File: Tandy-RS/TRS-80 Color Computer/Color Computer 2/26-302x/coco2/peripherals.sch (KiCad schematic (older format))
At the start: 44 parts, among them J1 Left Joystick, J2 Right Joystick, J3 RS232, J4 Cassette, J5 Conn_01x16_Female, K1 HB1-DC5V-H62, Q1 2N3055, U1 SC77527P, U2 6821, U3 SC77526, U7 6822

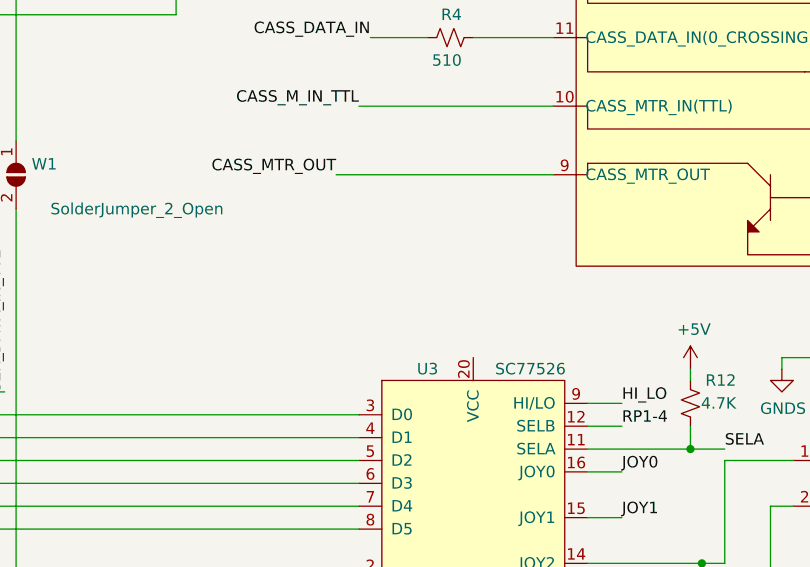
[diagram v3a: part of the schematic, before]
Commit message: connected all of the sheets
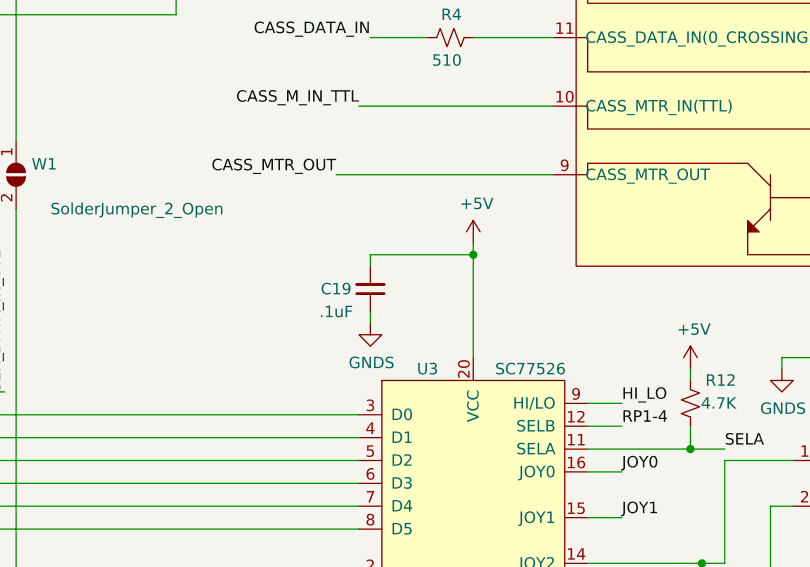
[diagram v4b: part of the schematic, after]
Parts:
- added C19: .1uF, Capacitor_THT:C_Axial_L3.8mm_D2.6mm_P10.00mm_Horizontal, symbol Device:C_Small
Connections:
- net +5V: now also U3.20 (VCC), C19.2
- net GNDS: now also C19.1
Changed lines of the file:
@@
 P 10000 1400
 AR Path="/602A51A8/60A871AE" Ref="#PWR?"  Part="1"
-AR Path="/603CF7B8/60A871AE" Ref="#PWR?"  Part="1"
-F 0 "#PWR?" H 10000 1150 50  0001 C CNN
+AR Path="/603CF7B8/60A871AE" Ref="#PWR0164"  Part="1"
+F 0 "#PWR0164" H 10000 1150 50  0001 C CNN
 F 1 "GNDS" H 10005 1227 50  0000 C CNN
 F 2 "" H 10000 1400 50  0001 C CNN
@@
 P 8850 4250
 AR Path="/602A51A8/60A871C7" Ref="#PWR?"  Part="1"
-AR Path="/603CF7B8/60A871C7" Ref="#PWR?"  Part="1"
-F 0 "#PWR?" H 8850 4000 50  0001 C CNN
+AR Path="/603CF7B8/60A871C7" Ref="#PWR0165"  Part="1"
+F 0 "#PWR0165" H 8850 4000 50  0001 C CNN
 F 1 "GNDS" H 8855 4077 50  0000 C CNN
 F 2 "" H 8850 4250 50  0001 C CNN
@@
 P 9400 2800
 AR Path="/602A51A8/60A871CF" Ref="#PWR?"  Part="1"
-AR Path="/603CF7B8/60A871CF" Ref="#PWR?"  Part="1"
-F 0 "#PWR?" H 9400 2550 50  0001 C CNN
+AR Path="/603CF7B8/60A871CF" Ref="#PWR0166"  Part="1"
+F 0 "#PWR0166" H 9400 2550 50  0001 C CNN
 F 1 "GNDS" H 9405 2627 50  0000 C CNN
 F 2 "" H 9400 2800 50  0001 C CNN
@@
 AR Path="/60273794/60A871FF" Ref="#PWR?"  Part="1"
 AR Path="/602A51A8/60A871FF" Ref="#PWR?"  Part="1"
-AR Path="/603CF7B8/60A871FF" Ref="#PWR?"  Part="1"
-F 0 "#PWR?" H 10400 2250 50  0001 C CNN
+AR Path="/603CF7B8/60A871FF" Ref="#PWR0167"  Part="1"
+F 0 "#PWR0167" H 10400 2250 50  0001 C CNN
 F 1 "+5V" H 10415 2573 50  0000 C CNN
 F 2 "" H 10400 2400 50  0001 C CNN
@@
 P 10250 2100
 AR Path="/602A51A8/60A87208" Ref="#FLG?"  Part="1"
-AR Path="/603CF7B8/60A87208" Ref="#FLG?"  Part="1"
-F 0 "#FLG?" H 10250 2175 50  0001 C CNN
+AR Path="/603CF7B8/60A87208" Ref="#FLG0101"  Part="1"
+F 0 "#FLG0101" H 10250 2175 50  0001 C CNN
 F 1 "PWR_FLAG" H 10250 2273 50  0000 C CNN
 F 2 "" H 10250 2100 50  0001 C CNN
@@
 P 3250 4050
 AR Path="/602A51A8/60BDD9E3" Ref="#PWR?"  Part="1"
-AR Path="/603CF7B8/60BDD9E3" Ref="#PWR?"  Part="1"
-F 0 "#PWR?" H 3250 3800 50  0001 C CNN
+AR Path="/603CF7B8/60BDD9E3" Ref="#PWR0168"  Part="1"
+F 0 "#PWR0168" H 3250 3800 50  0001 C CNN
 F 1 "GNDS" H 3255 3877 50  0000 C CNN
 F 2 "" H 3250 4050 50  0001 C CNN
@@
 AR Path="/60273794/60BE31ED" Ref="#PWR?"  Part="1"
 AR Path="/602A51A8/60BE31ED" Ref="#PWR?"  Part="1"
-AR Path="/603CF7B8/60BE31ED" Ref="#PWR?"  Part="1"
-F 0 "#PWR?" H 2950 650 50  0001 C CNN
+AR Path="/603CF7B8/60BE31ED" Ref="#PWR0169"  Part="1"
+F 0 "#PWR0169" H 2950 650 50  0001 C CNN
 F 1 "+5V" H 2965 973 50  0000 C CNN
 F 2 "" H 2950 800 50  0001 C CNN
@@
 P 4300 1300
 AR Path="/602A51A8/60CCA7E6" Ref="#PWR?"  Part="1"
-AR Path="/603CF7B8/60CCA7E6" Ref="#PWR?"  Part="1"
-F 0 "#PWR?" H 4300 1050 50  0001 C CNN
+AR Path="/603CF7B8/60CCA7E6" Ref="#PWR0170"  Part="1"
+F 0 "#PWR0170" H 4300 1050 50  0001 C CNN
 F 1 "GNDS" H 4150 1250 50  0000 C CNN
 F 2 "" H 4300 1300 50  0001 C CNN
@@
 AR Path="/60273794/60DBF928" Ref="#PWR?"  Part="1"
 AR Path="/602A51A8/60DBF928" Ref="#PWR?"  Part="1"
-AR Path="/603CF7B8/60DBF928" Ref="#PWR?"  Part="1"
-F 0 "#PWR?" H 600 6700 50  0001 C CNN
+AR Path="/603CF7B8/60DBF928" Ref="#PWR0171"  Part="1"
+F 0 "#PWR0171" H 600 6700 50  0001 C CNN
 F 1 "+5V" H 615 7023 50  0000 C CNN
 F 2 "" H 600 6850 50  0001 C CNN
@@
 P 2100 900
 AR Path="/602A51A8/60E75DAA" Ref="#PWR?"  Part="1"
-AR Path="/603CF7B8/60E75DAA" Ref="#PWR?"  Part="1"
-F 0 "#PWR?" H 2100 650 50  0001 C CNN
+AR Path="/603CF7B8/60E75DAA" Ref="#PWR0172"  Part="1"
+F 0 "#PWR0172" H 2100 650 50  0001 C CNN
 F 1 "GNDS" H 2105 727 50  0000 C CNN
 F 2 "" H 2100 900 50  0001 C CNN
@@
 AR Path="/60273794/60E8A73C" Ref="#PWR?"  Part="1"
 AR Path="/602A51A8/60E8A73C" Ref="#PWR?"  Part="1"
-AR Path="/603CF7B8/60E8A73C" Ref="#PWR?"  Part="1"
-F 0 "#PWR?" H 3000 4200 50  0001 C CNN
+AR Path="/603CF7B8/60E8A73C" Ref="#PWR0173"  Part="1"
+F 0 "#PWR0173" H 3000 4200 50  0001 C CNN
 F 1 "+5V" H 3015 4523 50  0000 C CNN
 F 2 "" H 3000 4350 50  0001 C CNN
@@
 P 2150 4450
 AR Path="/602A51A8/60E8A74F" Ref="#PWR?"  Part="1"
-AR Path="/603CF7B8/60E8A74F" Ref="#PWR?"  Part="1"
-F 0 "#PWR?" H 2150 4200 50  0001 C CNN
+AR Path="/603CF7B8/60E8A74F" Ref="#PWR0174"  Part="1"
+F 0 "#PWR0174" H 2150 4200 50  0001 C CNN
 F 1 "GNDS" H 2155 4277 50  0000 C CNN
 F 2 "" H 2150 4450 50  0001 C CNN
@@
 P 3000 7650
 AR Path="/602A51A8/60EC0CD2" Ref="#PWR?"  Part="1"
-AR Path="/603CF7B8/60EC0CD2" Ref="#PWR?"  Part="1"
-F 0 "#PWR?" H 3000 7400 50  0001 C CNN
+AR Path="/603CF7B8/60EC0CD2" Ref="#PWR0175"  Part="1"
+F 0 "#PWR0175" H 3000 7400 50  0001 C CNN
 F 1 "GNDS" H 3005 7477 50  0000 C CNN
 F 2 "" H 3000 7650 50  0001 C CNN
@@
 AR Path="/60273794/60EDF4D8" Ref="#PWR?"  Part="1"
 AR Path="/602A51A8/60EDF4D8" Ref="#PWR?"  Part="1"
-AR Path="/603CF7B8/60EDF4D8" Ref="#PWR?"  Part="1"
-F 0 "#PWR?" H 4400 5900 50  0001 C CNN
+AR Path="/603CF7B8/60EDF4D8" Ref="#PWR0176"  Part="1"
+F 0 "#PWR0176" H 4400 5900 50  0001 C CNN
 F 1 "+5V" H 4415 6223 50  0000 C CNN
 F 2 "" H 4400 6050 50  0001 C CNN
@@
 AR Path="/60273794/60F3326E" Ref="#PWR?"  Part="1"
 AR Path="/602A51A8/60F3326E" Ref="#PWR?"  Part="1"
-AR Path="/603CF7B8/60F3326E" Ref="#PWR?"  Part="1"
-F 0 "#PWR?" H 6950 4650 50  0001 C CNN
+AR Path="/603CF7B8/60F3326E" Ref="#PWR0177"  Part="1"
+F 0 "#PWR0177" H 6950 4650 50  0001 C CNN
 F 1 "+5V" H 6965 4973 50  0000 C CNN
 F 2 "" H 6950 4800 50  0001 C CNN
@@
 P 6000 6900
 AR Path="/602A51A8/611F4F3A" Ref="#PWR?"  Part="1"
-AR Path="/603CF7B8/611F4F3A" Ref="#PWR?"  Part="1"
-F 0 "#PWR?" H 6000 6650 50  0001 C CNN
+AR Path="/603CF7B8/611F4F3A" Ref="#PWR0178"  Part="1"
+F 0 "#PWR0178" H 6000 6650 50  0001 C CNN
 F 1 "GNDS" H 6005 6727 50  0000 C CNN
 F 2 "" H 6000 6900 50  0001 C CNN
@@
 P 7500 5700
 AR Path="/602A51A8/6126A799" Ref="#PWR?"  Part="1"
-AR Path="/603CF7B8/6126A799" Ref="#PWR?"  Part="1"
-F 0 "#PWR?" H 7500 5450 50  0001 C CNN
+AR Path="/603CF7B8/6126A799" Ref="#PWR0179"  Part="1"
+F 0 "#PWR0179" H 7500 5450 50  0001 C CNN
 F 1 "GNDS" H 7505 5527 50  0000 C CNN
 F 2 "" H 7500 5700 50  0001 C CNN
@@
 P 9200 6650
 AR Path="/602A51A8/61276EF8" Ref="#PWR?"  Part="1"
-AR Path="/603CF7B8/61276EF8" Ref="#PWR?"  Part="1"
-F 0 "#PWR?" H 9200 6400 50  0001 C CNN
+AR Path="/603CF7B8/61276EF8" Ref="#PWR0180"  Part="1"
+F 0 "#PWR0180" H 9200 6400 50  0001 C CNN
 F 1 "GNDS" H 9400 6600 50  0000 C CNN
 F 2 "" H 9200 6650 50  0001 C CNN
@@
 P 7150 6300
 AR Path="/602A51A8/612E73EA" Ref="#PWR?"  Part="1"
-AR Path="/603CF7B8/612E73EA" Ref="#PWR?"  Part="1"
-F 0 "#PWR?" H 7150 6050 50  0001 C CNN
+AR Path="/603CF7B8/612E73EA" Ref="#PWR0181"  Part="1"
+F 0 "#PWR0181" H 7150 6050 50  0001 C CNN
 F 1 "GNDS" H 7155 6127 50  0000 C CNN
 F 2 "" H 7150 6300 50  0001 C CNN
@@
 AR Path="/60273794/613E597B" Ref="#PWR?"  Part="1"
 AR Path="/602A51A8/613E597B" Ref="#PWR?"  Part="1"
-AR Path="/603CF7B8/613E597B" Ref="#PWR?"  Part="1"
-F 0 "#PWR?" H 9350 3250 50  0001 C CNN
+AR Path="/603CF7B8/613E597B" Ref="#PWR0182"  Part="1"
+F 0 "#PWR0182" H 9350 3250 50  0001 C CNN
 F 1 "+5V" H 9365 3573 50  0000 C CNN
 F 2 "" H 9350 3400 50  0001 C CNN
@@
 P 7350 4800
 AR Path="/602A51A8/61571302" Ref="#PWR?"  Part="1"
-AR Path="/603CF7B8/61571302" Ref="#PWR?"  Part="1"
-F 0 "#PWR?" H 7350 4550 50  0001 C CNN
+AR Path="/603CF7B8/61571302" Ref="#PWR0183"  Part="1"
+F 0 "#PWR0183" H 7350 4550 50  0001 C CNN
 F 1 "GNDS" H 7355 4627 50  0000 C CNN
 F 2 "" H 7350 4800 50  0001 C CNN
@@
 P 8750 4800
 AR Path="/602A51A8/615B1D6B" Ref="#PWR?"  Part="1"
-AR Path="/603CF7B8/615B1D6B" Ref="#PWR?"  Part="1"
-F 0 "#PWR?" H 8750 4550 50  0001 C CNN
+AR Path="/603CF7B8/615B1D6B" Ref="#PWR0184"  Part="1"
+F 0 "#PWR0184" H 8750 4550 50  0001 C CNN
 F 1 "GNDS" H 8755 4627 50  0000 C CNN
 F 2 "" H 8750 4800 50  0001 C CNN
@@
 Wire Wire Line
 	1100 5500 2500 5500
+$Comp
+L power:+5V #PWR?
+U 1 1 608F8DDD
+P 6000 4250
+AR Path="/60273794/608F8DDD" Ref="#PWR?"  Part="1"
+AR Path="/602A51A8/608F8DDD" Ref="#PWR?"  Part="1"
+AR Path="/603CF7B8/608F8DDD" Ref="#PWR0186"  Part="1"
+F 0 "#PWR0186" H 6000 4100 50  0001 C CNN
+F 1 "+5V" H 6015 4423 50  0000 C CNN
+F 2 "" H 6000 4250 50  0001 C CNN
+F 3 "" H 6000 4250 50  0001 C CNN
+	1    6000 4250
+	1    0    0    -1
+$EndComp
+$Comp
+L Device:C_Small C?
+U 1 1 60917560
+P 5550 4450
+AR Path="/60273794/60917560" Ref="C?"  Part="1"
+AR Path="/602A51A8/60917560" Ref="C?"  Part="1"
+AR Path="/603CF7B8/60917560" Ref="C19"  Part="1"
+F 0 "C19" H 5700 4450 50  0000 C CNN
+F 1 ".1uF" H 5700 4550 50  0000 C CNN
+F 2 "Capacitor_THT:C_Axial_L3.8mm_D2.6mm_P10.00mm_Horizontal" H 5550 4450 50  0001 C CNN
+F 3 "https://www.vishay.com/docs/45164/aseries.pdf" H 5550 4450 50  0001 C CNN
+F 4 "digikey" V 5550 4450 50  0001 C CNN "Vendor"
+F 5 "1109PHTR-ND" V 5550 4450 50  0001 C CNN "Vendor part#"
+F 6 "A104K15X7RF5TAA" V 5550 4450 50  0001 C CNN "Manufacturerer part #"
+	1    5550 4450
+	-1   0    0    1
+$EndComp
+Wire Wire Line
+	6000 4250 6000 4300
+Wire Wire Line
+	5550 4350 5550 4300
+Wire Wire Line
+	5550 4300 6000 4300
+Connection ~ 6000 4300
+Wire Wire Line
+	6000 4300 6000 4750
+$Comp
+L power:GNDS #PWR?
+U 1 1 6095624D
+P 5550 4600
+AR Path="/602A51A8/6095624D" Ref="#PWR?"  Part="1"
+AR Path="/603CF7B8/6095624D" Ref="#PWR0187"  Part="1"
+F 0 "#PWR0187" H 5550 4350 50  0001 C CNN
+F 1 "GNDS" H 5555 4427 50  0000 C CNN
+F 2 "" H 5550 4600 50  0001 C CNN
+F 3 "" H 5550 4600 50  0001 C CNN
+	1    5550 4600
+	1    0    0    -1
+$EndComp
+Wire Wire Line
+	5550 4550 5550 4600
 Wire Bus Line
 	1000 1150 1000 5400

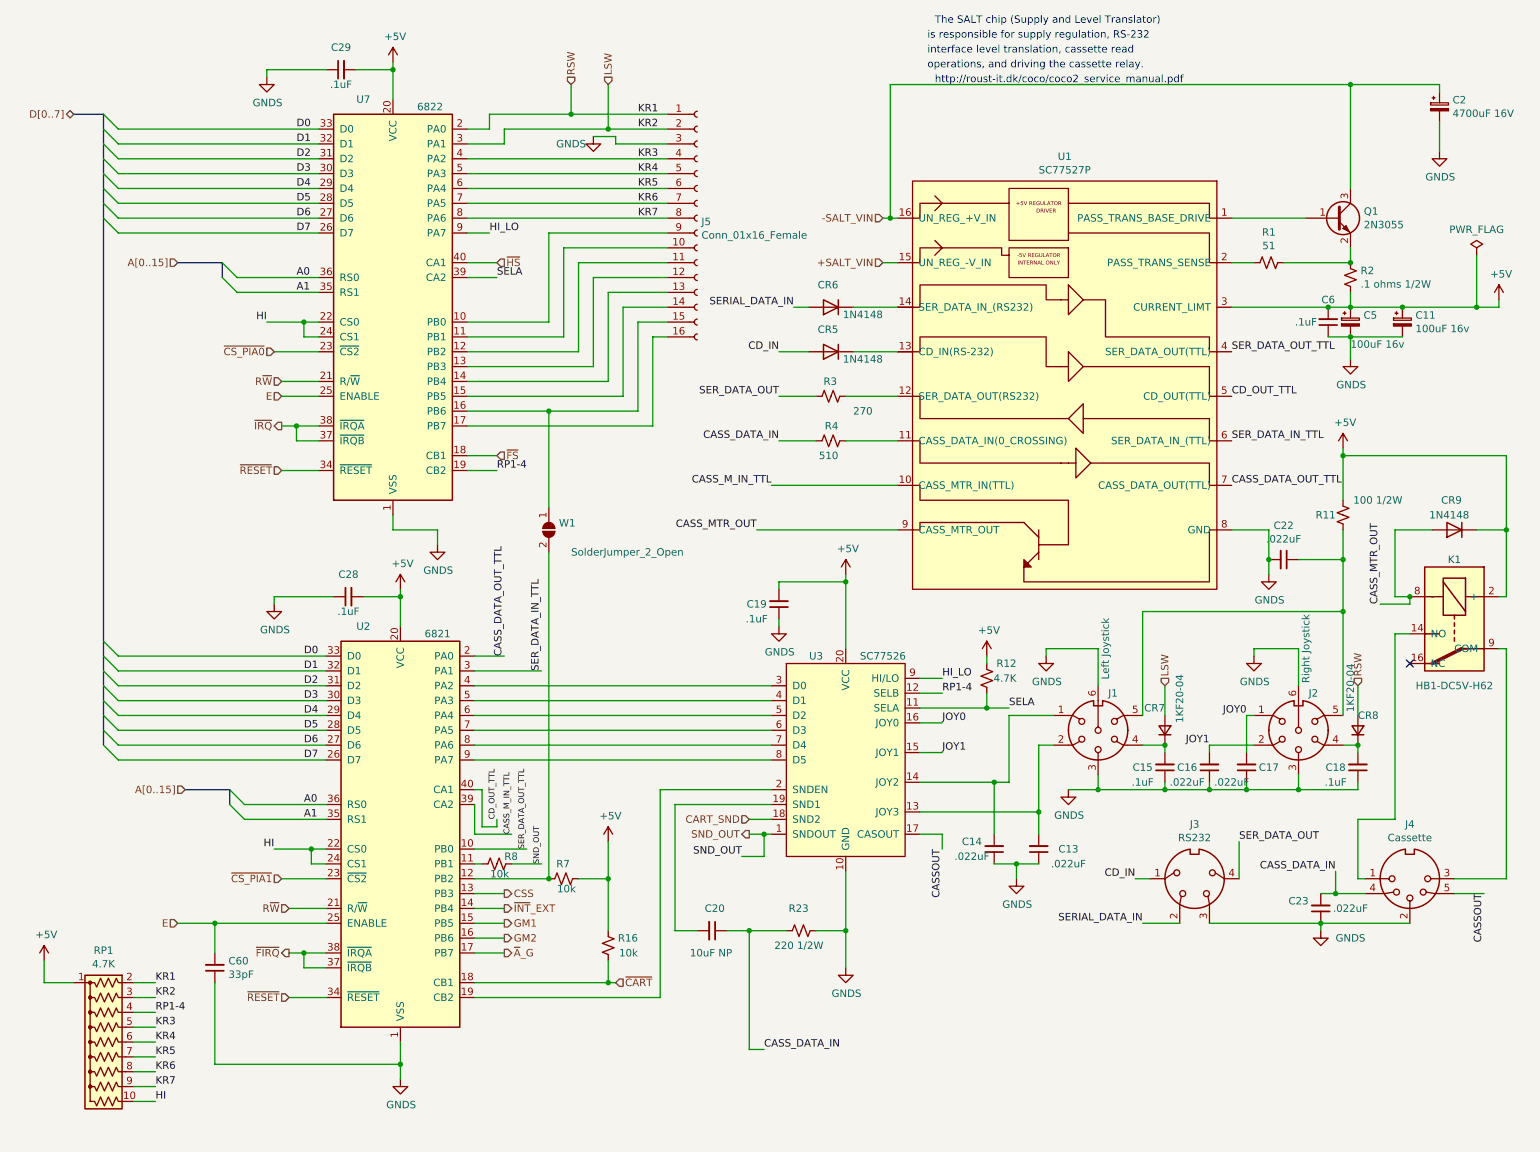
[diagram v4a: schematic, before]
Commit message: -Finished schematic. -Cleaned up schematic. -Added final footprint. -Started PCB
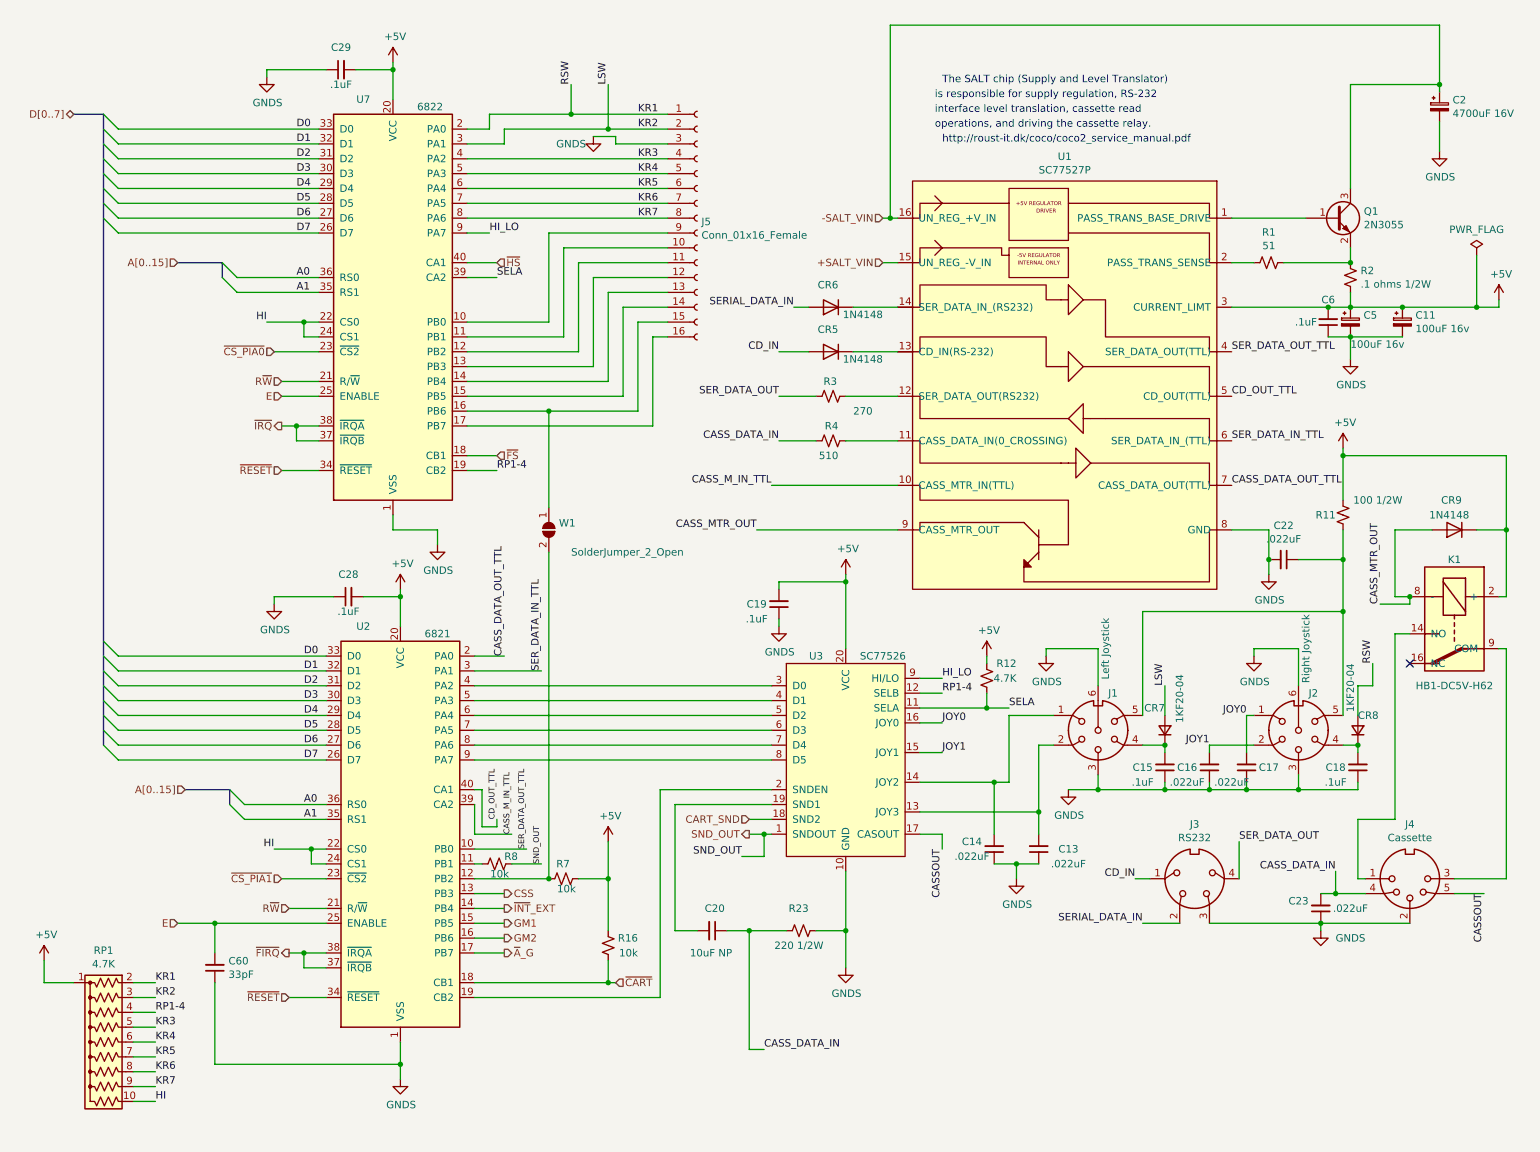
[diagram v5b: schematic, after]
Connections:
- net LSW renamed KR2
- net RSW renamed KR1
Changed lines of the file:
@@
 $Descr A 11000 8500
 encoding utf-8
-Sheet 8 8
+Sheet 7 8
 Title "TRS-80 Color Computer 2 (26-3026 & 26-30267)"
 Date "2021-02-20"
@@
 Wire Wire Line
 	10000 950  9400 950
-Connection ~ 9400 950
 $Comp
 L power:GNDS #PWR?
@@
 Wire Wire Line
 	10250 2450 9750 2450
-Text Notes 6600 550  0    50   ~ 0
+Text Notes 6650 950  0    50   ~ 0
 The SALT chip (Supply and Level Translator)
-Text Notes 6550 650  0    50   ~ 0
+Text Notes 6600 1050 0    50   ~ 0
  is responsible for supply regulation, RS-232
-Text Notes 6550 750  0    50   ~ 0
+Text Notes 6600 1150 0    50   ~ 0
  interface level translation, cassette read
-Text Notes 6550 850  0    50   ~ 0
+Text Notes 6600 1250 0    50   ~ 0
  operations, and driving the cassette relay.
-Text Notes 6600 950  0    50   ~ 0
+Text Notes 6650 1350 0    50   ~ 0
 http://roust-it.dk/coco/coco2_service_manual.pdf
 Text HLabel 6250 1850 0    50   Input ~ 0
@@
 Wire Wire Line
 	6350 2150 6250 2150
-Wire Wire Line
-	6300 1850 6300 950
 Connection ~ 6300 1850
 Wire Wire Line
 	6300 1850 6250 1850
-Wire Wire Line
-	6300 950  9400 950
 Wire Wire Line
 	3450 3250 4700 3250
@@
 Wire Wire Line
 	3650 3450 3450 3450
-Text HLabel 4150 950  1    50   Input ~ 0
-RSW
-Text HLabel 4400 950  1    50   Input ~ 0
-LSW
 Wire Wire Line
 	4150 950  4150 1150
@@
 Wire Wire Line
 	8000 5400 8150 5400
-Text HLabel 8150 5000 1    50   Input ~ 0
-LSW
 Wire Wire Line
 	8150 5000 8150 5200
@@
 Connection ~ 9050 5700
 Connection ~ 9450 5400
-Text HLabel 9450 5000 1    50   Input ~ 0
-RSW
 Wire Wire Line
 	9450 5000 9450 5200
@@
 Wire Wire Line
 	5550 4550 5550 4600
+Text Label 8150 5000 1    50   ~ 0
+LSW
+Text Label 9550 4850 1    50   ~ 0
+RSW
+Wire Wire Line
+	9450 5000 9550 5000
+Wire Wire Line
+	9550 5000 9550 4850
+Text Label 4150 950  1    50   ~ 0
+RSW
+Text Label 4400 950  1    50   ~ 0
+LSW
+Wire Wire Line
+	6300 550  10000 550
+Wire Wire Line
+	10000 550  10000 950
+Wire Wire Line
+	6300 550  6300 1850
 Wire Bus Line
 	1000 1150 1000 5400
+Connection ~ 10000 950
 $EndSCHEMATC
